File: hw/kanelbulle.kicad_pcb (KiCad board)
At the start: 2 copper layers, 82.4 x 88.4 mm, 76 parts, among them J1 USB, U1 LPC1114/302, U2 PCA9685, U3 ULN2003A, U4 ULN2003A, U5 ULN2003A

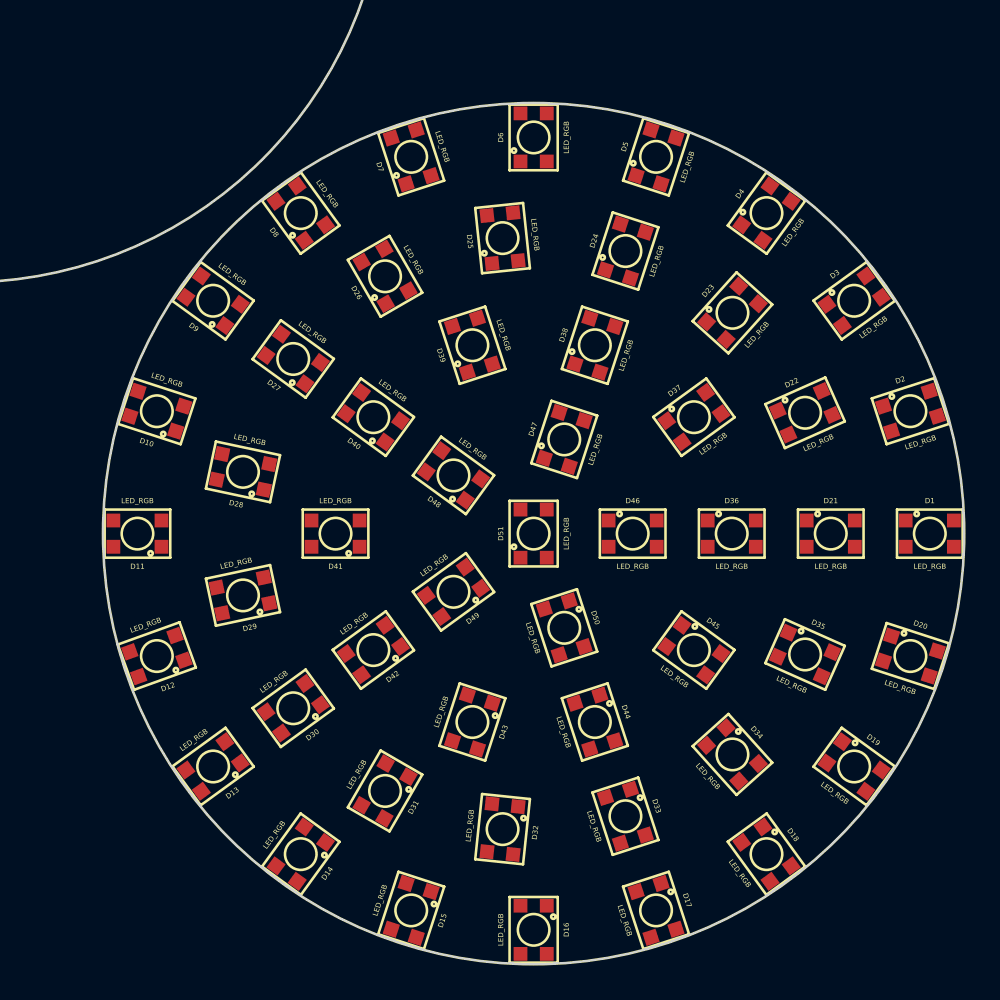
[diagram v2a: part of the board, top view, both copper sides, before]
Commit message: moved leds away from edge
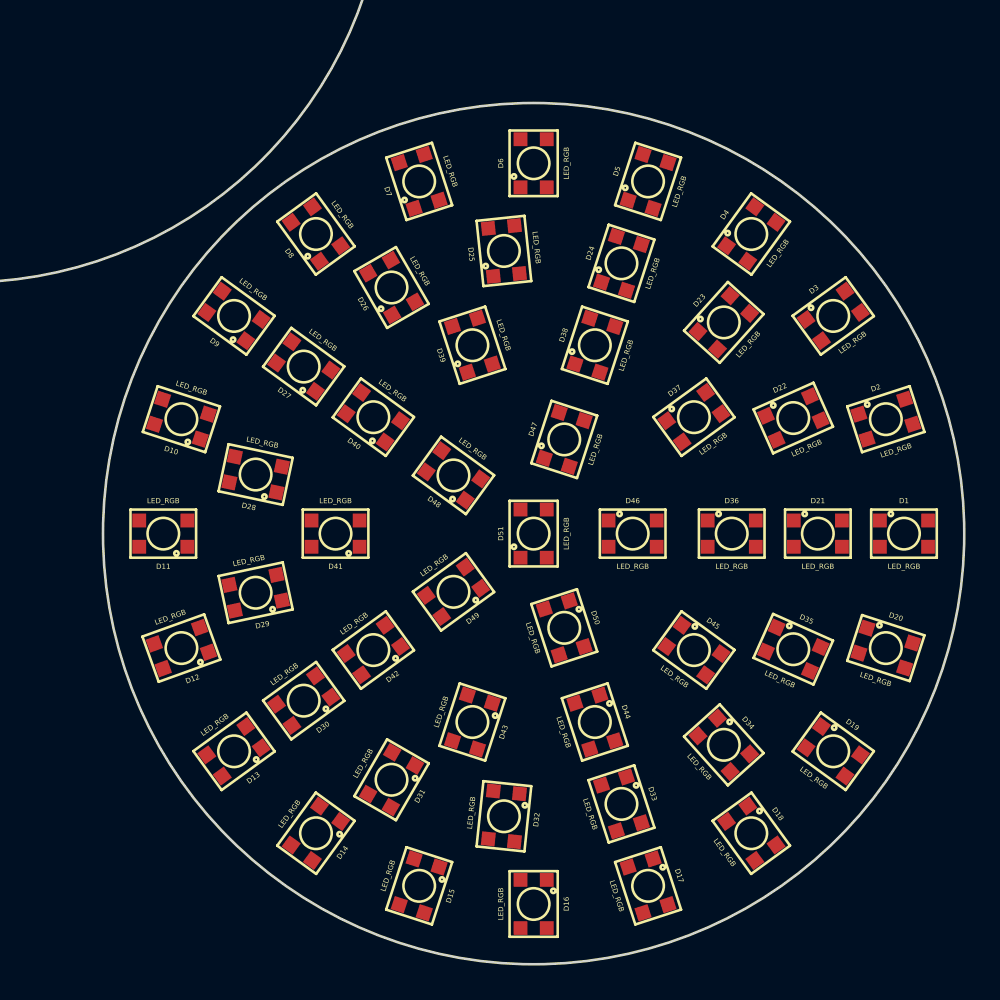
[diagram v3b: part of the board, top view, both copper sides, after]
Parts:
- moved D4 1.50 mm to (212.6, 132.6)
- moved D8 1.50 mm to (187.4, 132.6)
- moved D9 1.50 mm to (182.6, 137.4)
- moved D1 1.50 mm to (221.5, 150.0)
- moved D11 1.50 mm to (178.5, 150.0)
- moved D16 1.50 mm to (200.0, 171.5)
- moved D6 1.50 mm to (200.0, 128.5)
- moved D13 1.50 mm to (182.6, 162.6)
- moved D14 1.50 mm to (187.4, 167.4)
- moved D18 1.50 mm to (212.6, 167.4)
- moved D19 1.50 mm to (217.4, 162.6)
- moved D3 1.50 mm to (217.4, 137.4)
- moved D2 1.50 mm to (220.4, 143.4)
- moved D7 1.50 mm to (193.4, 129.6)
- moved D10 1.50 mm to (179.6, 143.4)
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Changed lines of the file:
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@@
     (links 246)
     (no_connects 246)
-    (area 142.511888 86.511888 225.075001 175.075001)
+    (area 125.477269 76.925001 225.183201 175.183201)
     (thickness 1.6)
     (drawings 8)
@@
   )
   (module PLCC4 (layer F.Cu)
-    (at 186.044 139.861 54)
+    (at 186.651 140.302 54)
     (fp_text reference D27 (at -1.905 0 144) (layer F.SilkS)
       (effects (font (size 0.3 0.3) (thickness 0.075)))
@@
   )
   (module PLCC4 (layer F.Cu)
-    (at 183.127 146.414 78)
+    (at 183.861 146.569 78)
     (fp_text reference D28 (at -1.905 0 168) (layer F.SilkS)
       (effects (font (size 0.3 0.3) (thickness 0.075)))
@@
   )
   (module PLCC4 (layer F.Cu)
-    (at 183.127 153.586 102)
+    (at 183.861 153.431 102)
     (fp_text reference D29 (at -1.905 0 192) (layer F.SilkS)
       (effects (font (size 0.3 0.3) (thickness 0.075)))
@@
   )
   (module PLCC4 (layer F.Cu)
-    (at 186.044 160.139 126)
+    (at 186.651 159.698 126)
     (fp_text reference D30 (at -1.905 0 216) (layer F.SilkS)
       (effects (font (size 0.3 0.3) (thickness 0.075)))
@@
   )
   (module PLCC4 (layer F.Cu)
-    (at 191.375 164.939 150)
+    (at 191.75 164.289 150)
     (fp_text reference D31 (at -1.905 0 240) (layer F.SilkS)
       (effects (font (size 0.3 0.3) (thickness 0.075)))
@@
   )
   (module PLCC4 (layer F.Cu)
-    (at 198.197 167.156 174)
+    (at 198.275 166.41 174)
     (fp_text reference D32 (at -1.905 0 264) (layer F.SilkS)
       (effects (font (size 0.3 0.3) (thickness 0.075)))
@@
   )
   (module PLCC4 (layer F.Cu)
-    (at 205.33 166.406 198)
+    (at 205.099 165.692 198)
     (fp_text reference D33 (at -1.905 0 288) (layer F.SilkS)
       (effects (font (size 0.3 0.3) (thickness 0.075)))
@@
   )
   (module PLCC4 (layer F.Cu)
-    (at 211.543 162.819 222)
+    (at 211.041 162.262 222)
     (fp_text reference D34 (at -1.905 0 312) (layer F.SilkS)
       (effects (font (size 0.3 0.3) (thickness 0.075)))
@@
   )
   (module PLCC4 (layer F.Cu)
-    (at 215.759 157.016 246)
+    (at 215.074 156.711 246)
     (fp_text reference D35 (at -1.905 0 336) (layer F.SilkS)
       (effects (font (size 0.3 0.3) (thickness 0.075)))
@@
   )
   (module PLCC4 (layer F.Cu)
-    (at 191.375 135.061 30)
+    (at 191.75 135.711 30)
     (fp_text reference D26 (at -1.905 0 120) (layer F.SilkS)
       (effects (font (size 0.3 0.3) (thickness 0.075)))
@@
   )
   (module PLCC4 (layer F.Cu)
-    (at 186.481 168.607 144)
+    (at 187.363 167.394 144)
     (fp_text reference D14 (at -1.905 0 234) (layer F.SilkS)
       (effects (font (size 0.3 0.3) (thickness 0.075)))
@@
   )
   (module PLCC4 (layer F.Cu)
-    (at 221.874 142.892 288)
+    (at 220.448 143.356 288)
     (fp_text reference D2 (at -1.905 0 378) (layer F.SilkS)
       (effects (font (size 0.3 0.3) (thickness 0.075)))
@@
   )
   (module PLCC4 (layer F.Cu)
-    (at 218.607 136.481 306)
+    (at 217.394 137.363 306)
     (fp_text reference D3 (at -1.905 0 396) (layer F.SilkS)
       (effects (font (size 0.3 0.3) (thickness 0.075)))
@@
   )
   (module PLCC4 (layer F.Cu)
-    (at 213.519 131.392 324)
+    (at 212.637 132.606 324)
     (fp_text reference D4 (at -1.905 0 414) (layer F.SilkS)
       (effects (font (size 0.3 0.3) (thickness 0.075)))
@@
   )
   (module PLCC4 (layer F.Cu)
-    (at 207.107 128.126 342)
+    (at 206.644 129.552 342)
     (fp_text reference D5 (at -1.905 0 432) (layer F.SilkS)
       (effects (font (size 0.3 0.3) (thickness 0.075)))
@@
   )
   (module PLCC4 (layer F.Cu)
-    (at 200 127)
+    (at 200 128.5)
     (fp_text reference D6 (at -1.905 0 90) (layer F.SilkS)
       (effects (font (size 0.3 0.3) (thickness 0.075)))
@@
   )
   (module PLCC4 (layer F.Cu)
-    (at 192.892 128.126 18)
+    (at 193.356 129.552 18)
     (fp_text reference D7 (at -1.905 0 108) (layer F.SilkS)
       (effects (font (size 0.3 0.3) (thickness 0.075)))
@@
   )
   (module PLCC4 (layer F.Cu)
-    (at 186.481 131.392 36)
+    (at 187.363 132.606 36)
     (fp_text reference D8 (at -1.905 0 126) (layer F.SilkS)
       (effects (font (size 0.3 0.3) (thickness 0.075)))
@@
   )
   (module PLCC4 (layer F.Cu)
-    (at 181.393 136.48 54)
+    (at 182.606 137.363 54)
     (fp_text reference D9 (at -1.905 0 144) (layer F.SilkS)
       (effects (font (size 0.3 0.3) (thickness 0.075)))
@@
   )
   (module PLCC4 (layer F.Cu)
-    (at 178.126 142.893 72)
+    (at 179.552 143.356 72)
     (fp_text reference D10 (at -1.905 0 162) (layer F.SilkS)
       (effects (font (size 0.3 0.3) (thickness 0.075)))
@@
   )
   (module PLCC4 (layer F.Cu)
-    (at 177 150 90)
+    (at 178.5 150 90)
     (fp_text reference D11 (at -1.905 0 180) (layer F.SilkS)
       (effects (font (size 0.3 0.3) (thickness 0.075)))
@@
   )
   (module PLCC4 (layer F.Cu)
-    (at 178.126 157.107 109.8)
+    (at 179.552 156.644 109.8)
     (fp_text reference D12 (at -1.905 0 199.8) (layer F.SilkS)
       (effects (font (size 0.3 0.3) (thickness 0.075)))
@@
   )
   (module PLCC4 (layer F.Cu)
-    (at 181.393 163.519 126)
+    (at 182.606 162.637 126)
     (fp_text reference D13 (at -1.905 0 216) (layer F.SilkS)
       (effects (font (size 0.3 0.3) (thickness 0.075)))
@@
   )
   (module PLCC4 (layer F.Cu)
-    (at 223 150 270)
+    (at 221.5 150 270)
     (fp_text reference D1 (at -1.905 0 360) (layer F.SilkS)
       (effects (font (size 0.3 0.3) (thickness 0.075)))
@@
   )
   (module PLCC4 (layer F.Cu)
-    (at 192.893 171.874 162)
+    (at 193.356 170.448 162)
     (fp_text reference D15 (at -1.905 0 252) (layer F.SilkS)
       (effects (font (size 0.3 0.3) (thickness 0.075)))
@@
   )
   (module PLCC4 (layer F.Cu)
-    (at 200 173 180)
+    (at 200 171.5 180)
     (fp_text reference D16 (at -1.905 0 270) (layer F.SilkS)
       (effects (font (size 0.3 0.3) (thickness 0.075)))
@@
   )
   (module PLCC4 (layer F.Cu)
-    (at 207.107 171.874 198)
+    (at 206.644 170.448 198)
     (fp_text reference D17 (at -1.905 0 288) (layer F.SilkS)
       (effects (font (size 0.3 0.3) (thickness 0.075)))
@@
   )
   (module PLCC4 (layer F.Cu)
-    (at 213.519 168.607 216)
+    (at 212.637 167.394 216)
     (fp_text reference D18 (at -1.905 0 306) (layer F.SilkS)
       (effects (font (size 0.3 0.3) (thickness 0.075)))
@@
   )
   (module PLCC4 (layer F.Cu)
-    (at 218.607 163.519 234)
+    (at 217.394 162.637 234)
     (fp_text reference D19 (at -1.905 0 324) (layer F.SilkS)
       (effects (font (size 0.3 0.3) (thickness 0.075)))
@@
   )
   (module PLCC4 (layer F.Cu)
-    (at 221.874 157.107 252)
+    (at 220.448 156.644 252)
     (fp_text reference D20 (at -1.905 0 342) (layer F.SilkS)
       (effects (font (size 0.3 0.3) (thickness 0.075)))
@@
   )
   (module PLCC4 (layer F.Cu)
-    (at 217.25 150 270)
+    (at 216.5 150 270)
     (fp_text reference D21 (at -1.905 0 360) (layer F.SilkS)
       (effects (font (size 0.3 0.3) (thickness 0.075)))
@@
   )
   (module PLCC4 (layer F.Cu)
-    (at 215.759 142.984 294)
+    (at 215.074 143.289 294)
     (fp_text reference D22 (at -1.905 0 384) (layer F.SilkS)
       (effects (font (size 0.3 0.3) (thickness 0.075)))
@@
   )
   (module PLCC4 (layer F.Cu)
-    (at 211.543 137.181 318)
+    (at 211.041 137.738 318)
     (fp_text reference D23 (at -1.905 0 408) (layer F.SilkS)
       (effects (font (size 0.3 0.3) (thickness 0.075)))
@@
   )
   (module PLCC4 (layer F.Cu)
-    (at 205.33 133.594 342)
+    (at 205.099 134.308 342)
     (fp_text reference D24 (at -1.905 0 432) (layer F.SilkS)
       (effects (font (size 0.3 0.3) (thickness 0.075)))
@@
   )
   (module PLCC4 (layer F.Cu)
-    (at 198.197 132.844 6)
+    (at 198.275 133.59 6)
     (fp_text reference D25 (at -1.905 0 96) (layer F.SilkS)
       (effects (font (size 0.3 0.3) (thickness 0.075)))

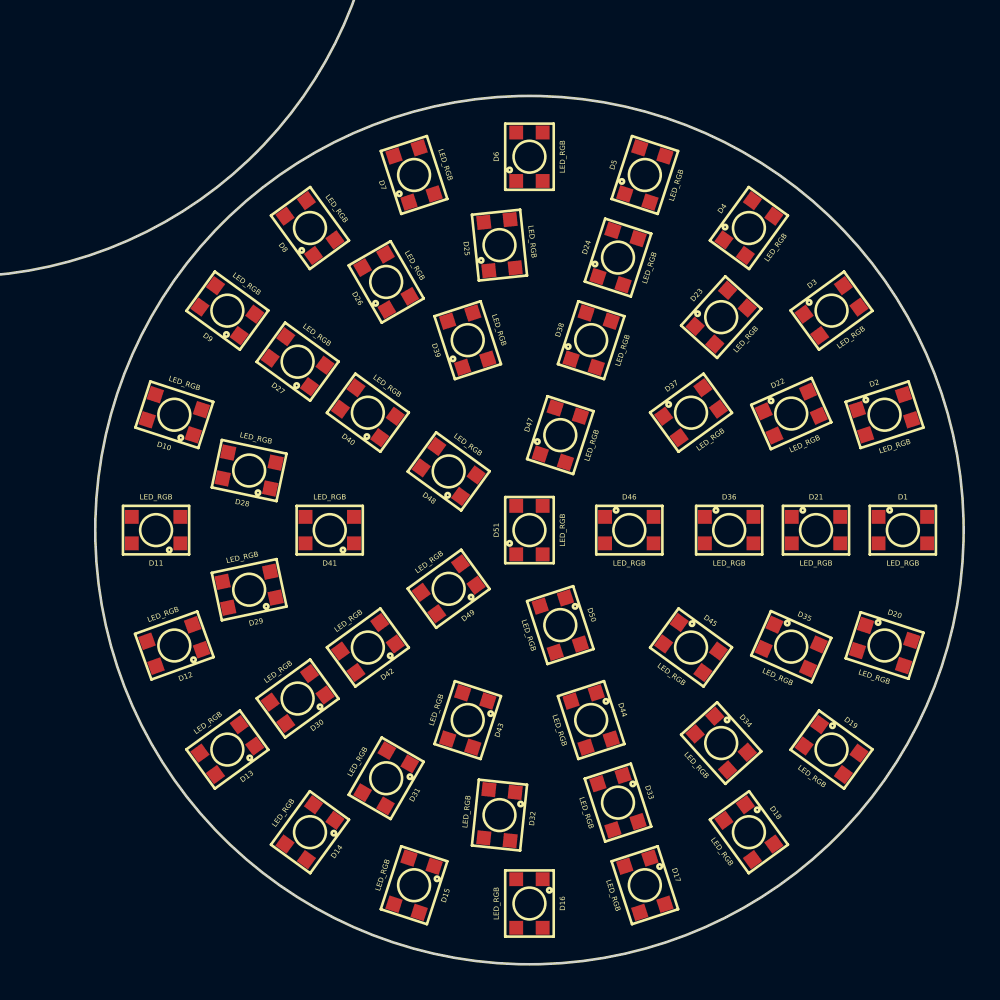
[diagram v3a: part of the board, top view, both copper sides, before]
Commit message: connected leds to eachother
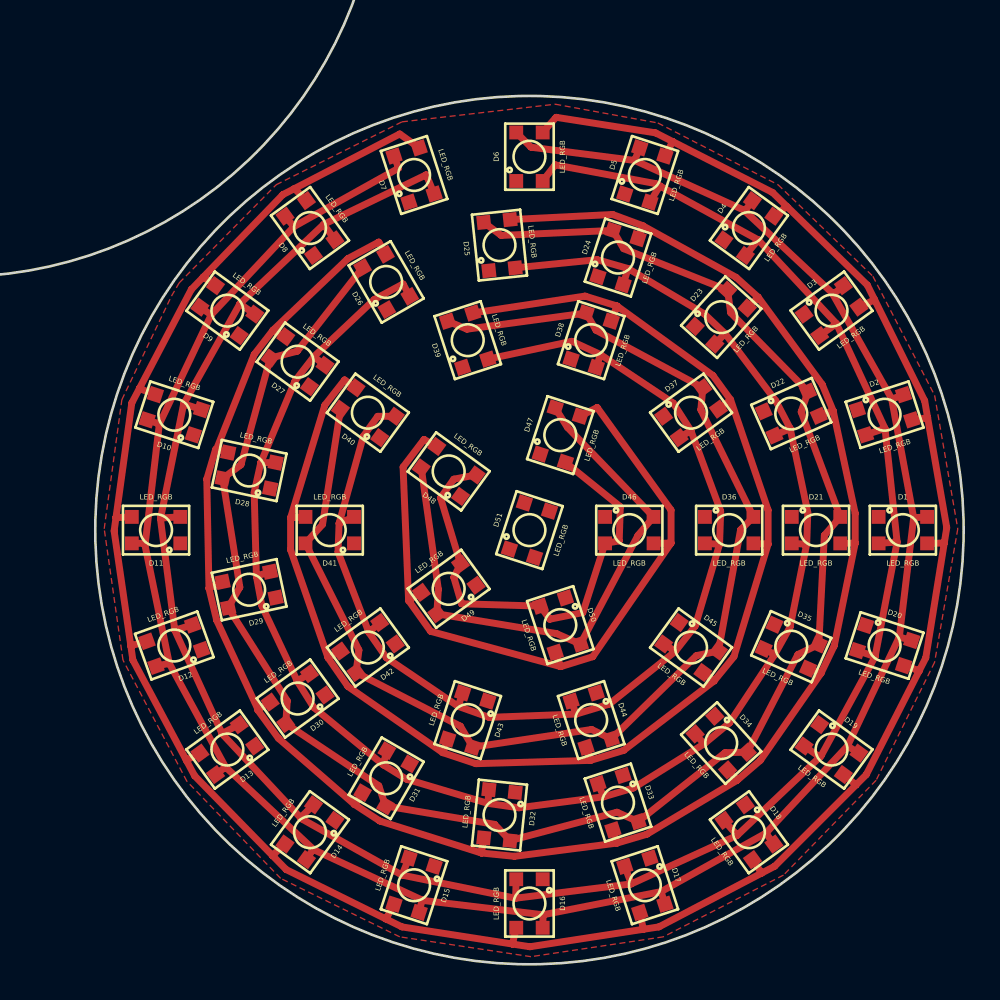
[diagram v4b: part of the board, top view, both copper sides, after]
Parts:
- turned D51 to 342 degrees
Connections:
- D20 pad 2: (no net) -> /R1
- D20 pad 3: (no net) -> /G1
- D20 pad 4: (no net) -> /B1
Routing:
- net /G1: track 0.00 -> 160.6 mm
- net /R1: track 0.00 -> 147.6 mm
- net /B1: track 0.00 -> 146.5 mm
- net /G2: track 0.00 -> 121.2 mm
- net /B2: track 0.00 -> 107.5 mm
- net /R2: track 0.00 -> 105.2 mm
- net /G3: track 0.00 -> 84.7 mm
- net /B3: track 0.00 -> 73.4 mm
- net /R3: track 0.00 -> 68.7 mm
- net /G4: track 0.00 -> 43.4 mm
- net /B4: track 0.00 -> 33.9 mm
- net /R4: track 0.00 -> 27.5 mm
- added copper zone on F.Cu, net 3V3
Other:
- net class led added: clearance 0.2032, trace_width 0.4, via_dia 0.95, via_drill 0.75
